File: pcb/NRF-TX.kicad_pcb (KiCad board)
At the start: 2 copper layers, 13 parts, among them J1 Conn_02x04_Odd_Even, J5 Conn_02x03_Odd_Even, U1 LM1117-3.3, U2 LM1117-5.0, U3 ATmega328-AU, Y1 Crystal

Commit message: added the layers
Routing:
- net GND: track 40.6 -> 43.2 mm, vias 4 -> 5
- net Net-(J1-Pad3): track 14.6 -> 15.7 mm
- net Net-(J5-Pad2): track 66.1 -> 66.4 mm, vias 0 -> 1
- added copper zone on B.Cu, net GND
- added copper zone on F.Cu, net Net-(C1-Pad1)
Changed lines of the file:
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@@
     (thickness 1.6)
     (drawings 0)
-    (tracks 176)
+    (tracks 191)
     (zones 0)
     (modules 13)
@@
   (segment (start 124.6 78.35) (end 124.6 78.35) (width 0.35) (layer F.Cu) (net 2))
   (via (at 124.6 78.35) (size 0.8) (drill 0.4) (layers F.Cu B.Cu) (net 2))
+  (segment (start 151.1875 89.75) (end 151.1875 91.9375) (width 0.35) (layer F.Cu) (net 2))
+  (segment (start 151.1875 91.9375) (end 151.5 92.25) (width 0.35) (layer F.Cu) (net 2))
+  (segment (start 151.5 92.25) (end 151.5 92.25) (width 0.35) (layer F.Cu) (net 2))
+  (via (at 151.5 92.25) (size 0.8) (drill 0.4) (layers F.Cu B.Cu) (net 2))
   (segment (start 133.6875 82.0875) (end 133.7 82.1) (width 0.5) (layer F.Cu) (net 3))
   (segment (start 133.6875 78.75) (end 133.6875 82.0875) (width 0.5) (layer F.Cu) (net 3))
@@
   (segment (start 145.04 79.29) (end 145.04 80.75) (width 0.35) (layer B.Cu) (net 8))
   (segment (start 144.75 79) (end 145.04 79.29) (width 0.35) (layer B.Cu) (net 8))
-  (segment (start 140.71 83.29) (end 140 84) (width 0.35) (layer F.Cu) (net 9))
-  (segment (start 131.5 82.5) (end 129.25 82.5) (width 0.35) (layer F.Cu) (net 9))
-  (segment (start 142.5 83.29) (end 140.71 83.29) (width 0.35) (layer F.Cu) (net 9))
-  (segment (start 140 84) (end 132.25 84) (width 0.35) (layer F.Cu) (net 9))
-  (segment (start 132.25 84) (end 131.75 83.5) (width 0.35) (layer F.Cu) (net 9))
-  (segment (start 131.75 83.5) (end 131.75 82.75) (width 0.35) (layer F.Cu) (net 9))
-  (segment (start 131.75 82.75) (end 131.5 82.5) (width 0.35) (layer F.Cu) (net 9))
+  (segment (start 141 83.97217) (end 141 83.75) (width 0.35) (layer F.Cu) (net 9))
+  (segment (start 141 83.75) (end 141.46 83.29) (width 0.35) (layer F.Cu) (net 9))
+  (segment (start 140.37219 84.59998) (end 141 83.97217) (width 0.35) (layer F.Cu) (net 9))
+  (segment (start 131.5 82.5) (end 131.75 82.75) (width 0.35) (layer F.Cu) (net 9))
+  (segment (start 141.46 83.29) (end 142.5 83.29) (width 0.35) (layer F.Cu) (net 9))
+  (segment (start 132.377821 84.59998) (end 140.37219 84.59998) (width 0.35) (layer F.Cu) (net 9))
+  (segment (start 129.25 82.5) (end 131.5 82.5) (width 0.35) (layer F.Cu) (net 9))
+  (segment (start 131.75 82.75) (end 131.75 84.25) (width 0.35) (layer F.Cu) (net 9))
+  (segment (start 132.127831 84.34999) (end 132.377821 84.59998) (width 0.35) (layer F.Cu) (net 9))
+  (segment (start 131.75 84.25) (end 131.84999 84.34999) (width 0.35) (layer F.Cu) (net 9))
+  (segment (start 131.84999 84.34999) (end 132.127831 84.34999) (width 0.35) (layer F.Cu) (net 9))
   (segment (start 145.04 83.29) (end 146.46 83.29) (width 0.35) (layer F.Cu) (net 10))
   (segment (start 146.46 83.29) (end 146.75 83) (width 0.35) (layer F.Cu) (net 10))
@@
   (segment (start 129.25 84.9) (end 131.90001 84.9) (width 0.35) (layer F.Cu) (net 12))
   (segment (start 144.83 85.83) (end 145.04 85.83) (width 0.35) (layer F.Cu) (net 12))
-  (segment (start 132.25 84.55001) (end 143.55001 84.55001) (width 0.35) (layer F.Cu) (net 12))
-  (segment (start 131.90001 84.9) (end 132.25 84.55001) (width 0.35) (layer F.Cu) (net 12))
+  (segment (start 131.90001 84.90001) (end 132.14999 85.14999) (width 0.35) (layer F.Cu) (net 12))
+  (segment (start 131.90001 84.9) (end 131.90001 84.90001) (width 0.35) (layer F.Cu) (net 12))
+  (segment (start 132.14999 85.14999) (end 140.60001 85.14999) (width 0.35) (layer F.Cu) (net 12))
+  (segment (start 143.495021 84.604999) (end 143.55001 84.55001) (width 0.35) (layer F.Cu) (net 12))
+  (segment (start 141.145001 84.604999) (end 143.495021 84.604999) (width 0.35) (layer F.Cu) (net 12))
+  (segment (start 140.60001 85.14999) (end 141.145001 84.604999) (width 0.35) (layer F.Cu) (net 12))
   (segment (start 151.54 80.29) (end 151.54 81.75) (width 0.5) (layer F.Cu) (net 13))
   (segment (start 150.9625 78.25) (end 150.9625 79.7125) (width 0.5) (layer F.Cu) (net 13))
   (segment (start 150.9625 79.7125) (end 151.54 80.29) (width 0.5) (layer F.Cu) (net 13))
   (segment (start 123 79.299998) (end 123 80.25) (width 0.35) (layer F.Cu) (net 13))
-  (segment (start 147.5 91) (end 146.5 92) (width 0.35) (layer F.Cu) (net 13))
-  (segment (start 153.5 82.25) (end 153.5 90) (width 0.35) (layer F.Cu) (net 13))
-  (segment (start 151.54 81.75) (end 153 81.75) (width 0.35) (layer F.Cu) (net 13))
-  (segment (start 141.25 92) (end 140.974999 92.275001) (width 0.35) (layer F.Cu) (net 13))
   (segment (start 139.55001 92.05001) (end 119.80001 92.05001) (width 0.35) (layer F.Cu) (net 13))
-  (segment (start 153 81.75) (end 153.5 82.25) (width 0.35) (layer F.Cu) (net 13))
-  (segment (start 139.775001 92.275001) (end 139.55001 92.05001) (width 0.35) (layer F.Cu) (net 13))
+  (segment (start 139.775001 92.275001) (end 139.775001 92.275001) (width 0.35) (layer F.Cu) (net 13))
   (segment (start 119.25 79.5) (end 119.675001 79.074999) (width 0.35) (layer F.Cu) (net 13))
-  (segment (start 146.5 92) (end 141.25 92) (width 0.35) (layer F.Cu) (net 13))
-  (segment (start 153.5 90) (end 152.5 91) (width 0.35) (layer F.Cu) (net 13))
-  (segment (start 140.974999 92.275001) (end 139.775001 92.275001) (width 0.35) (layer F.Cu) (net 13))
-  (segment (start 152.5 91) (end 147.5 91) (width 0.35) (layer F.Cu) (net 13))
   (segment (start 119.80001 92.05001) (end 119.25 91.5) (width 0.35) (layer F.Cu) (net 13))
   (segment (start 119.25 91.5) (end 119.25 79.5) (width 0.35) (layer F.Cu) (net 13))
   (segment (start 119.675001 79.074999) (end 122.775001 79.074999) (width 0.35) (layer F.Cu) (net 13))
   (segment (start 122.775001 79.074999) (end 123 79.299998) (width 0.35) (layer F.Cu) (net 13))
+  (segment (start 139.775001 92.275001) (end 139.55001 92.05001) (width 0.35) (layer F.Cu) (net 13))
+  (via (at 139.775001 92.275001) (size 0.8) (drill 0.4) (layers F.Cu B.Cu) (net 13))
+  (segment (start 142.474999 92.275001) (end 139.775001 92.275001) (width 0.35) (layer B.Cu) (net 13))
+  (segment (start 142.69999 92.05001) (end 142.474999 92.275001) (width 0.35) (layer B.Cu) (net 13))
+  (segment (start 146.727821 92.05001) (end 142.69999 92.05001) (width 0.35) (layer B.Cu) (net 13))
+  (segment (start 147.30001 91.477821) (end 146.727821 92.05001) (width 0.35) (layer B.Cu) (net 13))
+  (segment (start 153 81.75) (end 153.25 82) (width 0.35) (layer B.Cu) (net 13))
+  (segment (start 153.25 82) (end 153.25 90.5) (width 0.35) (layer B.Cu) (net 13))
+  (segment (start 151.54 81.75) (end 153 81.75) (width 0.35) (layer B.Cu) (net 13))
+  (segment (start 153.25 90.5) (end 152.75 91) (width 0.35) (layer B.Cu) (net 13))
+  (segment (start 152.75 91) (end 147.30001 91) (width 0.35) (layer B.Cu) (net 13))
+  (segment (start 147.30001 91) (end 147.30001 91.477821) (width 0.35) (layer B.Cu) (net 13))
   (segment (start 122.2 89.9) (end 122.25 89.95) (width 0.35) (layer F.Cu) (net 14))
   (segment (start 122.2 88.75) (end 122.2 89.9) (width 0.35) (layer F.Cu) (net 14))
@@
   (segment (start 140.5 91.5) (end 146.5 91.5) (width 0.35) (layer B.Cu) (net 14))
   (segment (start 146.5 91.5) (end 146.75 91.25) (width 0.35) (layer B.Cu) (net 14))
+  (zone (net 1) (net_name "Net-(C1-Pad1)") (layer F.Cu) (hatch edge 0.508)
+    (connect_pads yes (clearance 0.35))
+    (min_thickness 0.254)
+    (fill yes (arc_segments 32) (thermal_gap 0.35) (thermal_bridge_width 0.35))
+    (polygon
+      (pts
+        (xy 153.75 93.75) (xy 118 93.75) (xy 118 76) (xy 153.75 76)
+      )
+    )
+  )
+  (zone (net 2) (net_name GND) (layer B.Cu) (hatch edge 0.508)
+    (connect_pads yes (clearance 0.35))
+    (min_thickness 0.254)
+    (fill yes (arc_segments 32) (thermal_gap 0.35) (thermal_bridge_width 0.35))
+    (polygon
+      (pts
+        (xy 153.75 93.75) (xy 118 93.75) (xy 118 76) (xy 153.75 76)
+      )
+    )
+  )
 )

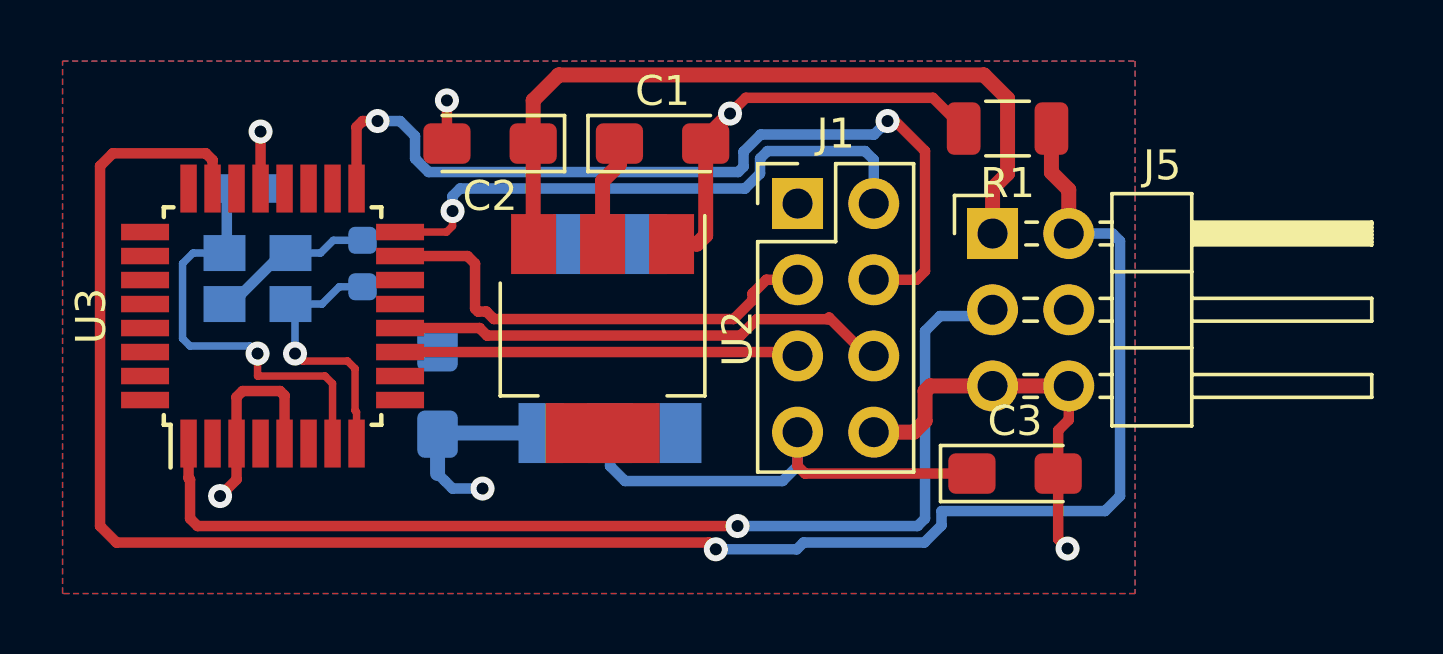
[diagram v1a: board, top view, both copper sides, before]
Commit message: added the edge cuts on the PCB
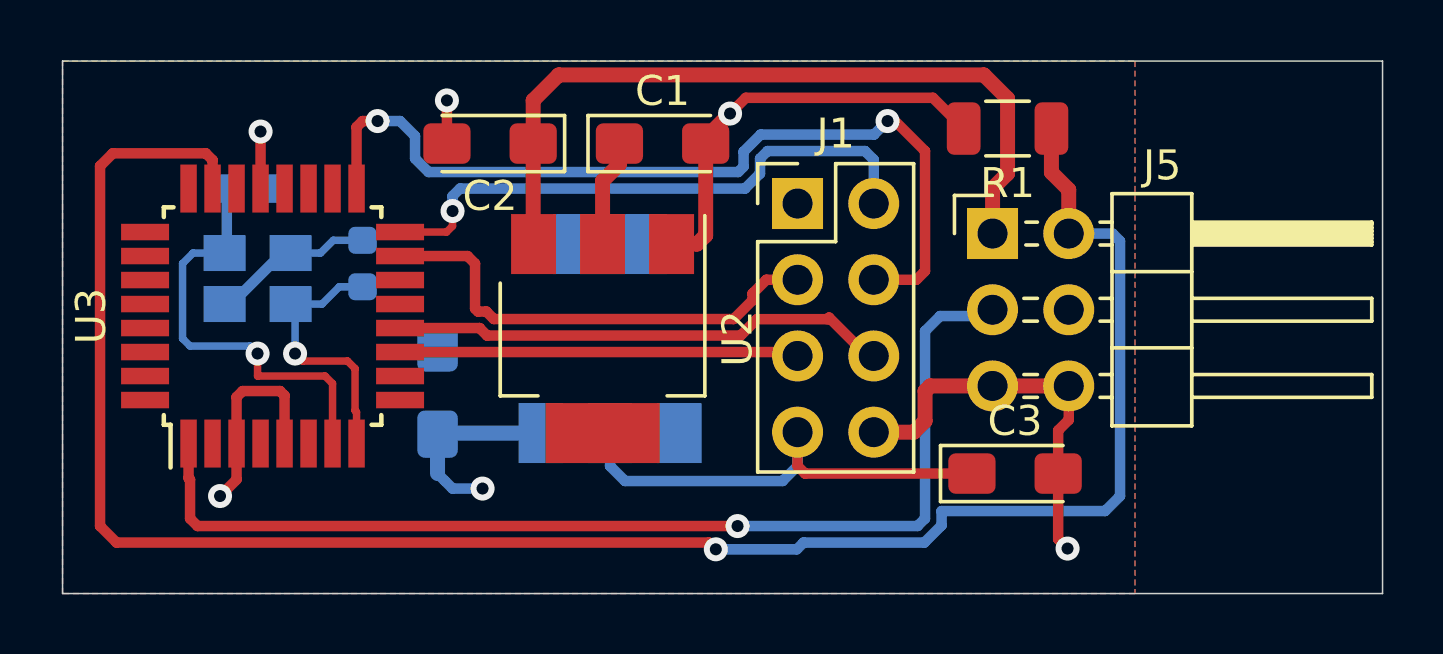
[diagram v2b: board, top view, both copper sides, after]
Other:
- board outline added: 44 x 17.8 mm
